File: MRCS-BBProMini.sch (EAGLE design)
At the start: 10 parts

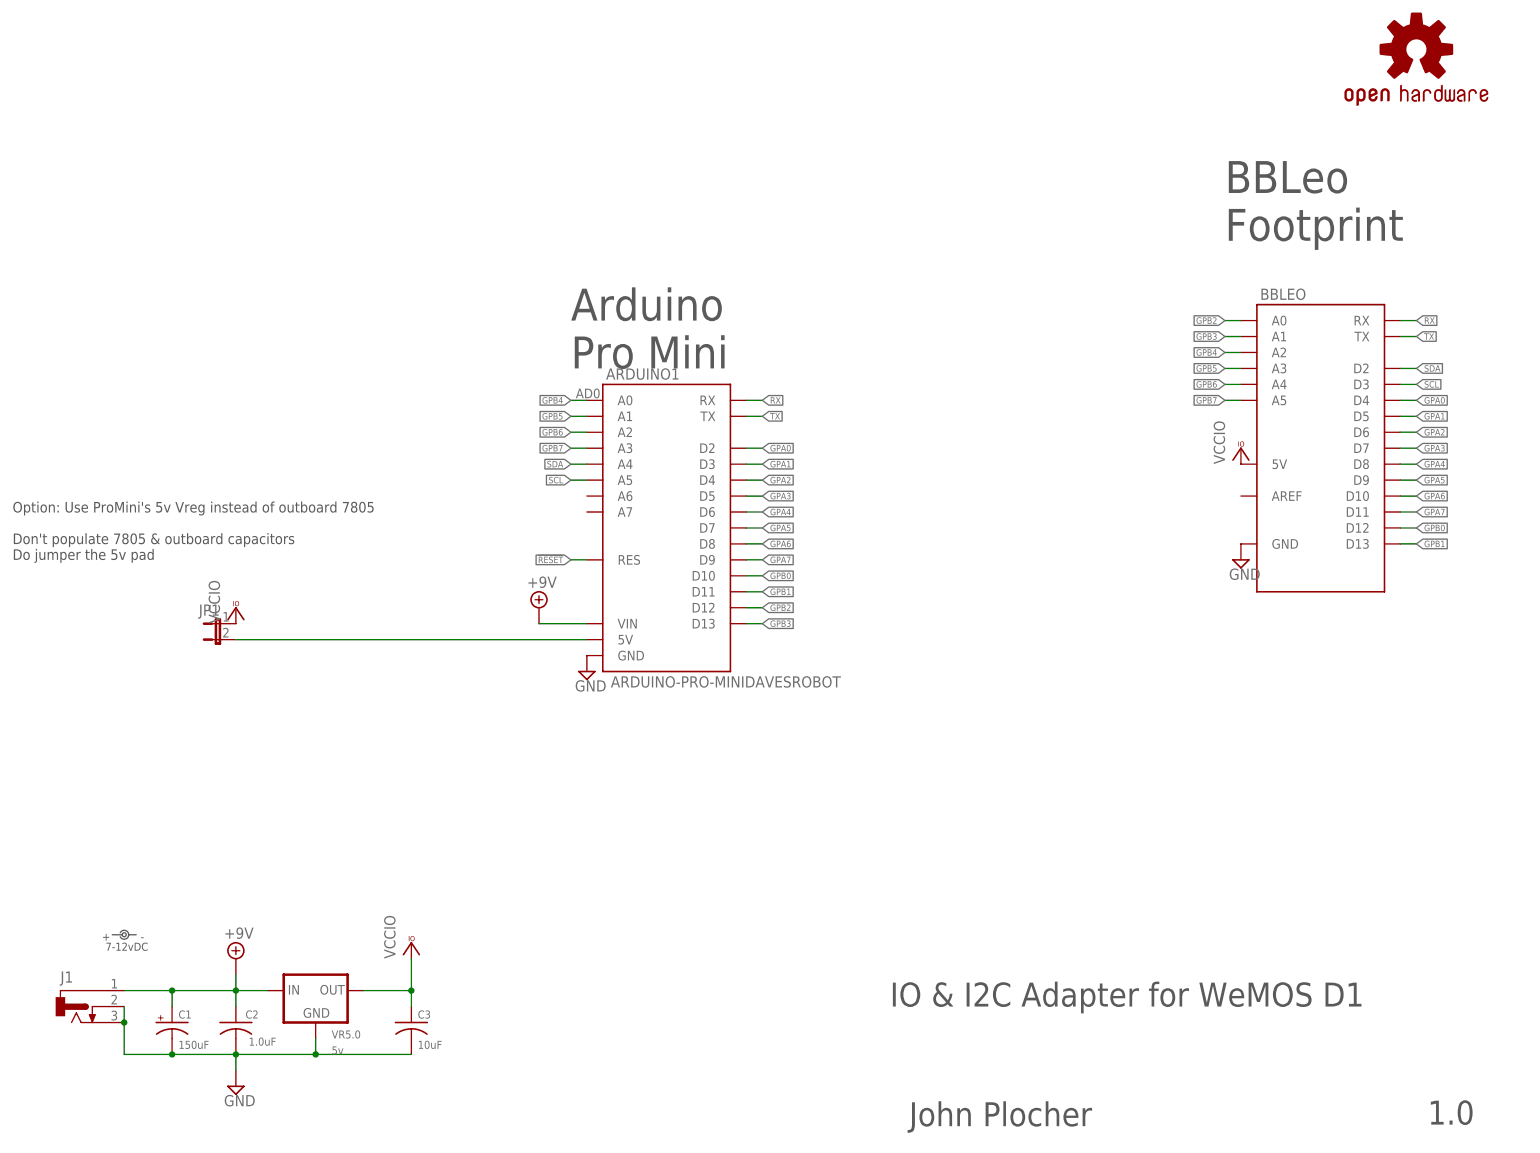
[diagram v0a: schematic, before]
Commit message: fixed silkscreen
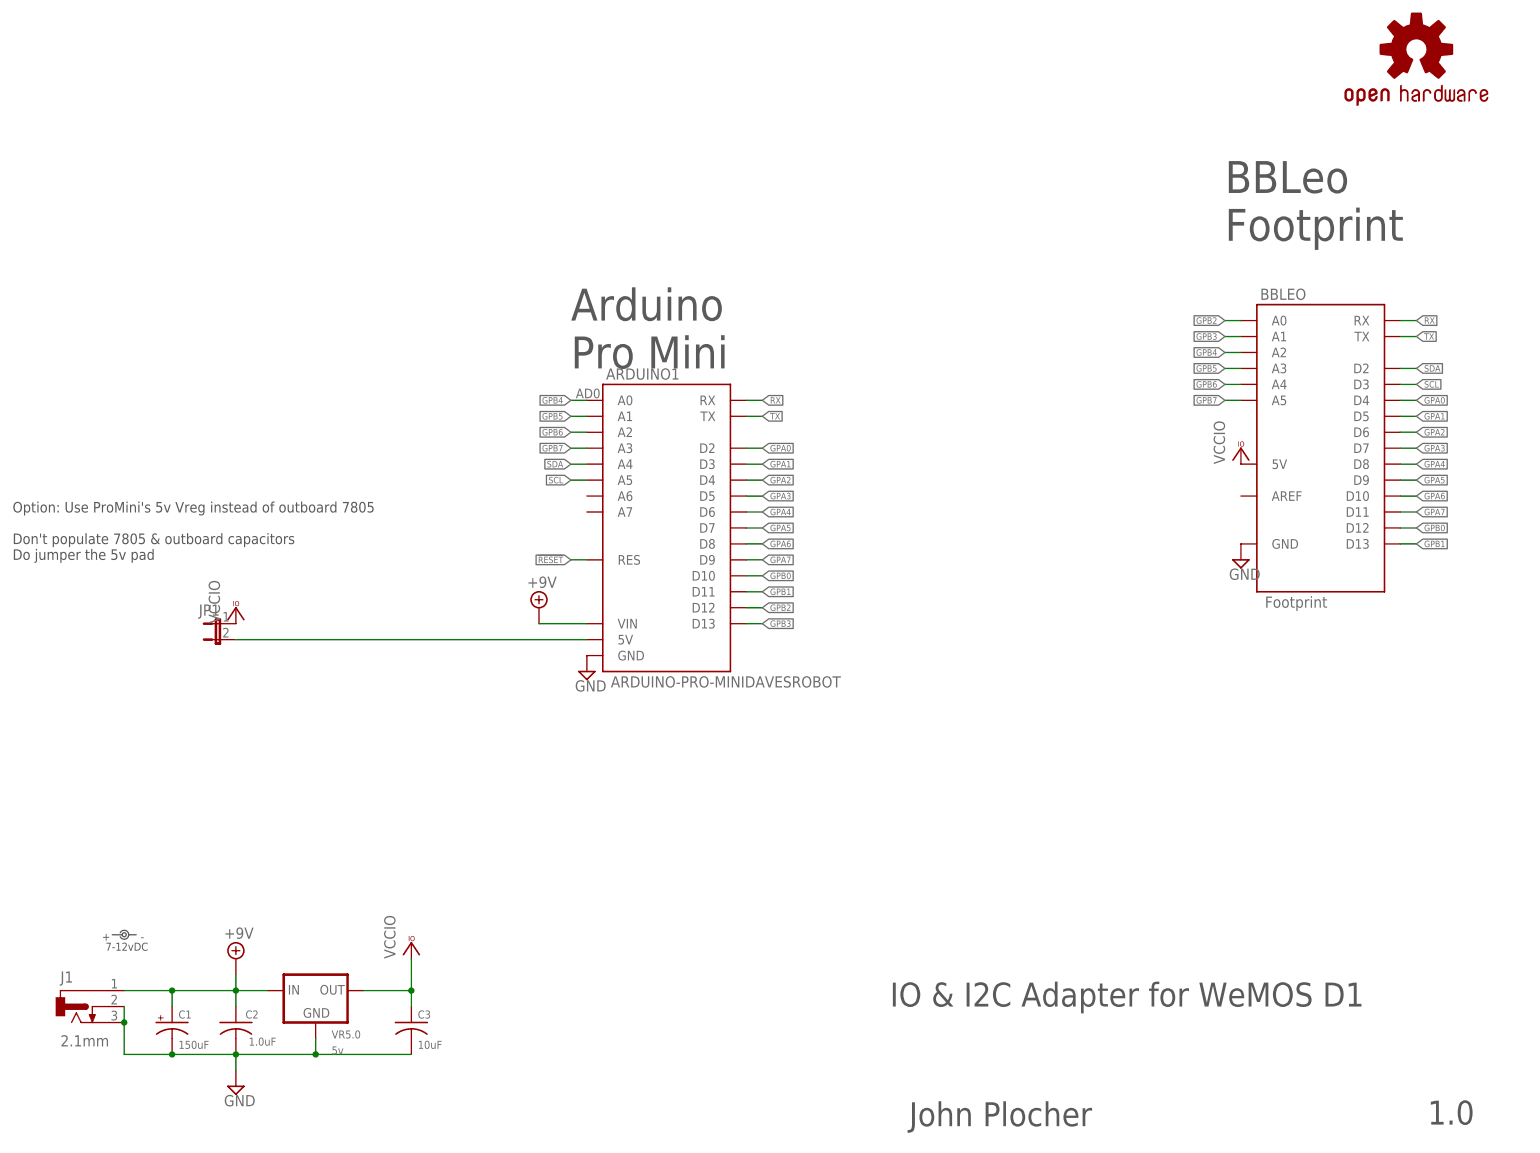
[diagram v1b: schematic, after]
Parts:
- BBLEO: value (none) -> Footprint
- J1: value (none) -> 2.1mm
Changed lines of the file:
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@@
 <part name="SUPPLY2" library="supply2" deviceset="+9V" device=""/>
 <part name="V12" library="supply2" deviceset="GND" device=""/>
-<part name="J1" library="SPCoast" deviceset="CONNECTOR-DC-POWER" device="-RA"/>
+<part name="J1" library="SPCoast" deviceset="CONNECTOR-DC-POWER" device="-RA" value="2.1mm"/>
 <part name="LABEL1" library="SPCoast" deviceset="DOC-POWER_LABEL" device="" value="7-12vDC"/>
 <part name="C3" library="SPCoast" deviceset="CAP*" device="PTH1" value="10uF"/>
@@
 <part name="VCC8" library="supply1" deviceset="VCCIO" device=""/>
 <part name="C1" library="SPCoast" deviceset="CAP-POL*" device="PTH-5MM" value="150uF"/>
-<part name="BBLEO" library="SPCoast" deviceset="ARDUINO-BBLEO" device=""/>
+<part name="BBLEO" library="SPCoast" deviceset="ARDUINO-BBLEO" device="" value="Footprint"/>
 <part name="V2" library="supply2" deviceset="GND" device=""/>
 <part name="VCC3" library="supply1" deviceset="VCCIO" device=""/>

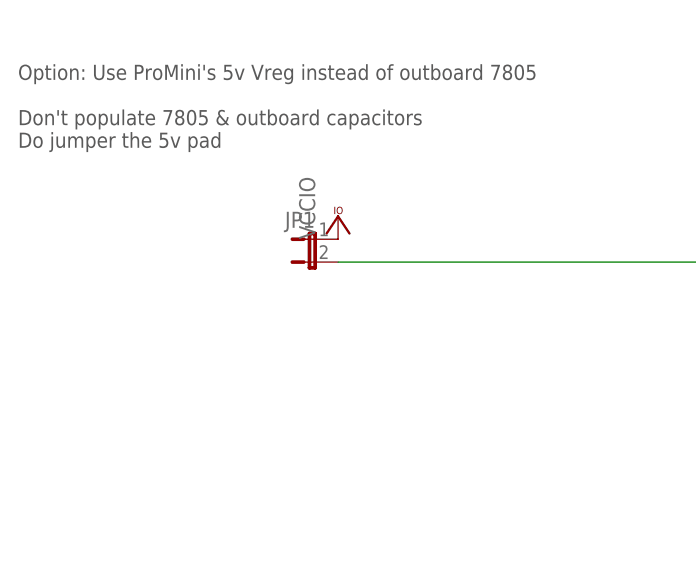
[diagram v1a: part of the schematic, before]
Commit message: fixed silkscreen
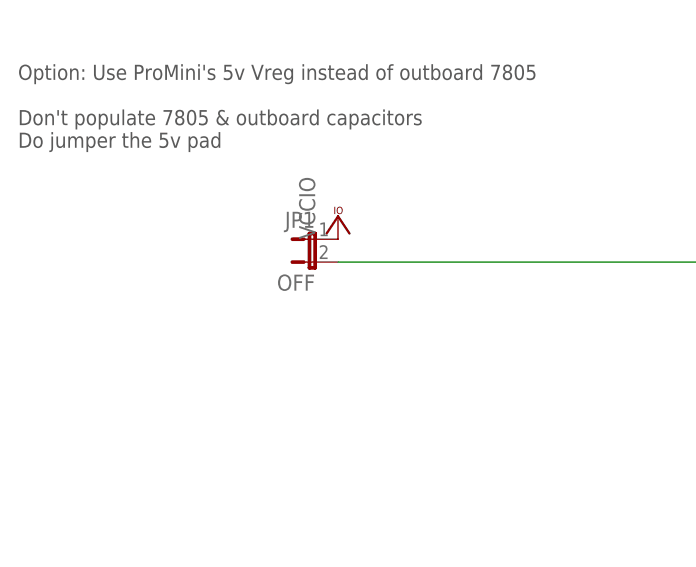
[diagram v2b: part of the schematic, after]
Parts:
- JP1: value (none) -> OFF
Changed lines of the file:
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@@
 <part name="V1" library="supply2" deviceset="GND" device=""/>
 <part name="SUPPLY1" library="supply2" deviceset="+9V" device=""/>
-<part name="JP1" library="SPCoast" deviceset="JUMPER-2" device="SMD-NO"/>
+<part name="JP1" library="SPCoast" deviceset="JUMPER-2" device="SMD-NO" value="OFF"/>
 <part name="VCC1" library="supply1" deviceset="VCCIO" device=""/>
 </parts>

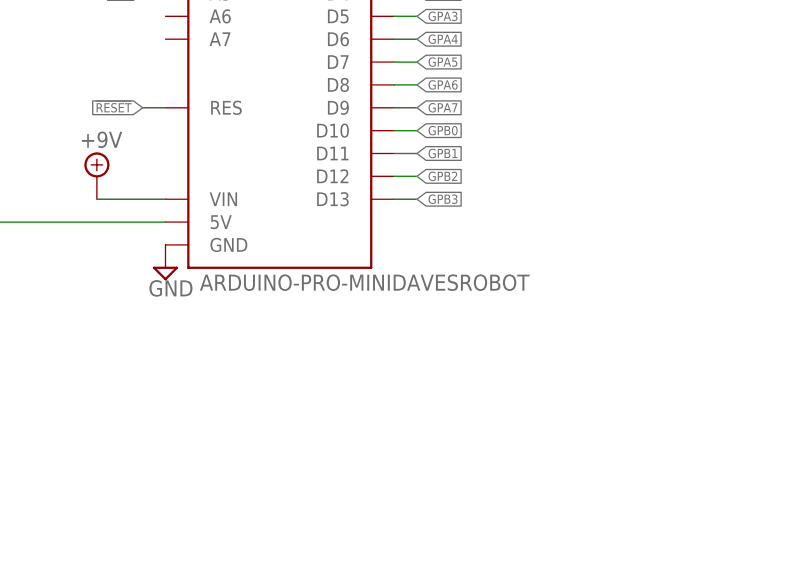
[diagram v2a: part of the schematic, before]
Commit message: normalized values
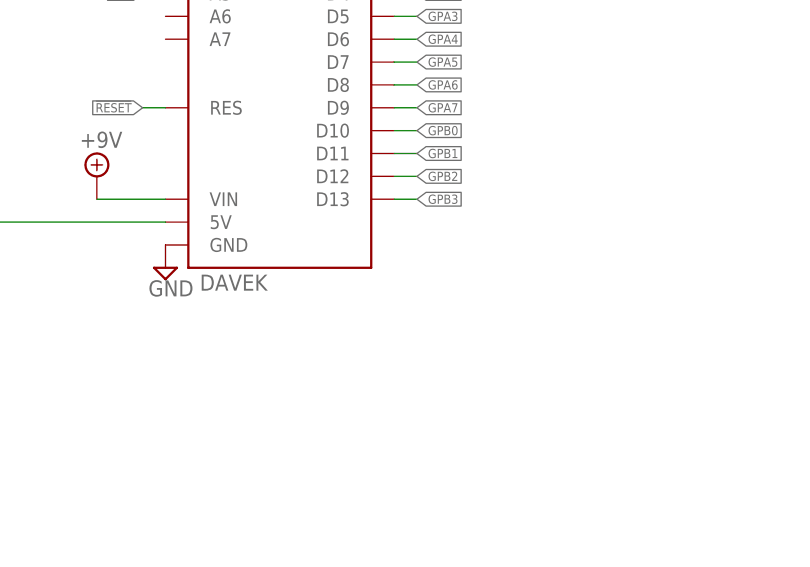
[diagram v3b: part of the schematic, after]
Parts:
- ARDUINO1: value ARDUINO-PRO-MINIDAVESROBOT -> DAVEK
- OSHW1: value DOC-OSHW-LOGO-M -> OSHW
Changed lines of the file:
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@@
 <parts>
 <part name="FRAME1" library="MCP" deviceset="FRAME-LETTER" device=""/>
-<part name="OSHW1" library="SPCoast" deviceset="DOC-OSHW-LOGO-" device="M" value="DOC-OSHW-LOGO-M"/>
+<part name="OSHW1" library="SPCoast" deviceset="DOC-OSHW-LOGO-" device="M" value="OSHW"/>
 <part name="SUPPLY2" library="supply2" deviceset="+9V" device=""/>
 <part name="V12" library="supply2" deviceset="GND" device=""/>
@@
 <part name="V2" library="supply2" deviceset="GND" device=""/>
 <part name="VCC3" library="supply1" deviceset="VCCIO" device=""/>
-<part name="ARDUINO1" library="SPCoast" deviceset="ARDUINO-PRO-MINI" device="DAVESROBOT"/>
+<part name="ARDUINO1" library="SPCoast" deviceset="ARDUINO-PRO-MINI" device="DAVESROBOT" value="DAVEK"/>
 <part name="V1" library="supply2" deviceset="GND" device=""/>
 <part name="SUPPLY1" library="supply2" deviceset="+9V" device=""/>
